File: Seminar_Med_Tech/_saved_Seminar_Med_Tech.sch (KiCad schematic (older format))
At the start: 86 parts, among them U1 JP26, U10 JP27, U11 JP28, U12 JP29, U13 JP30, U14 ADS1298, U15 JP31, U16 JP32, U17 JP33, U18 ADS1298, U19 OPA2340, U2 JP27, U20 J5, U3 JP28, U4 JP29, U5 JP30, U6 JP31, U7 JP32, U8 JP33, U9 JP26

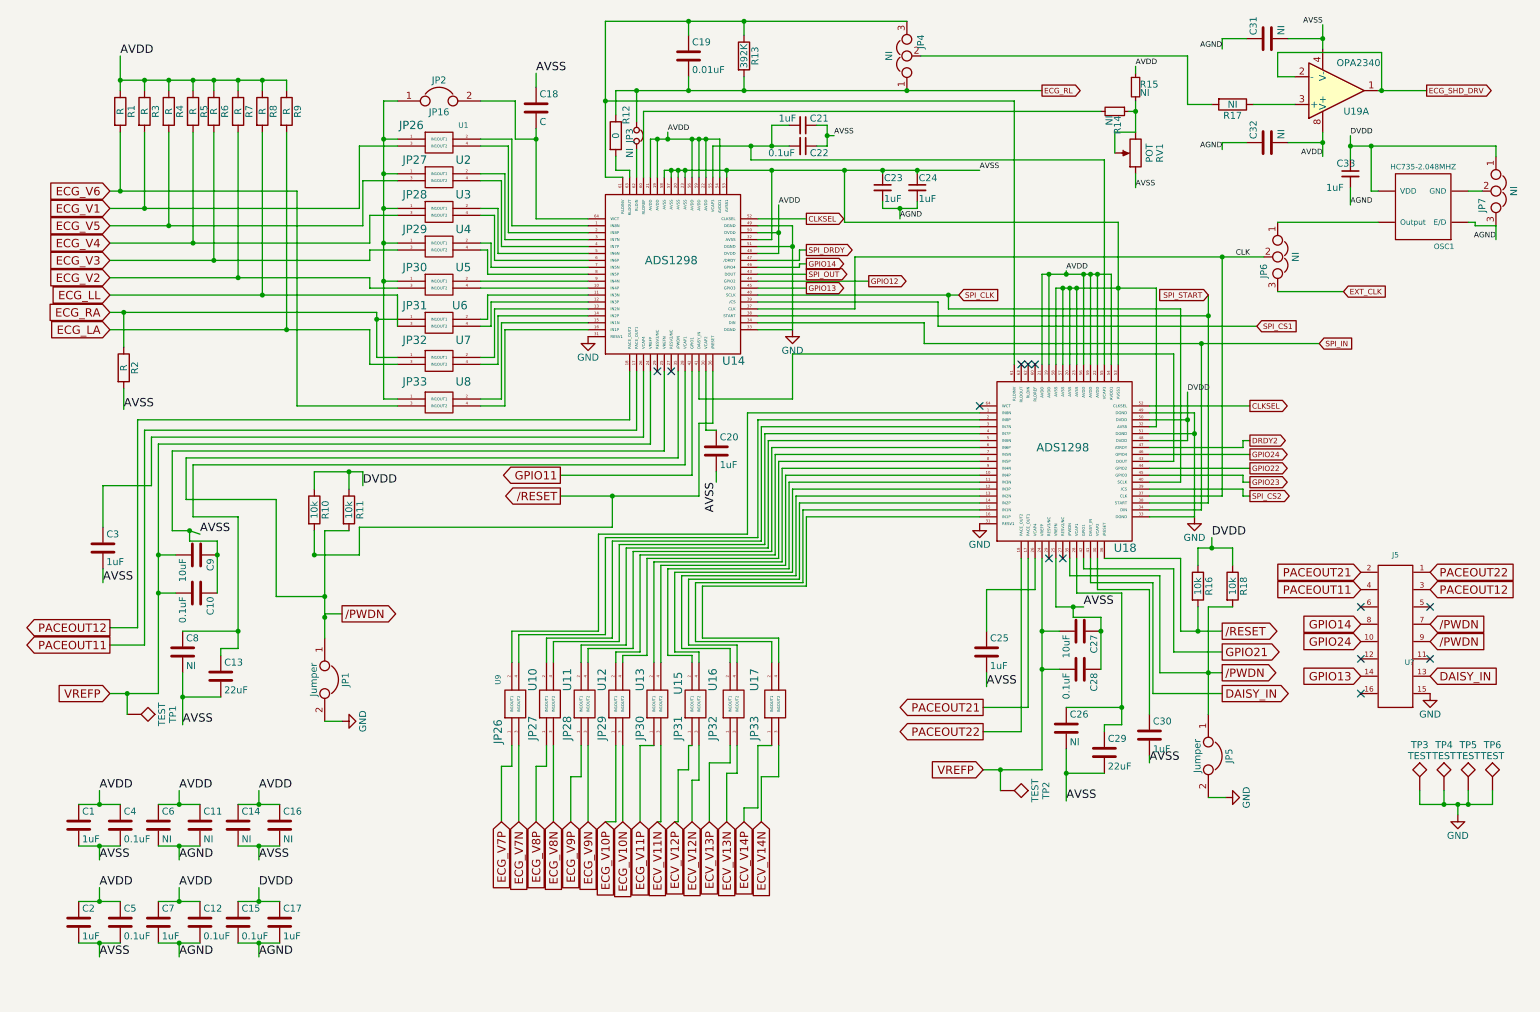
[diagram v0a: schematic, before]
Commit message: Updated Dokumentation and Schaltbild
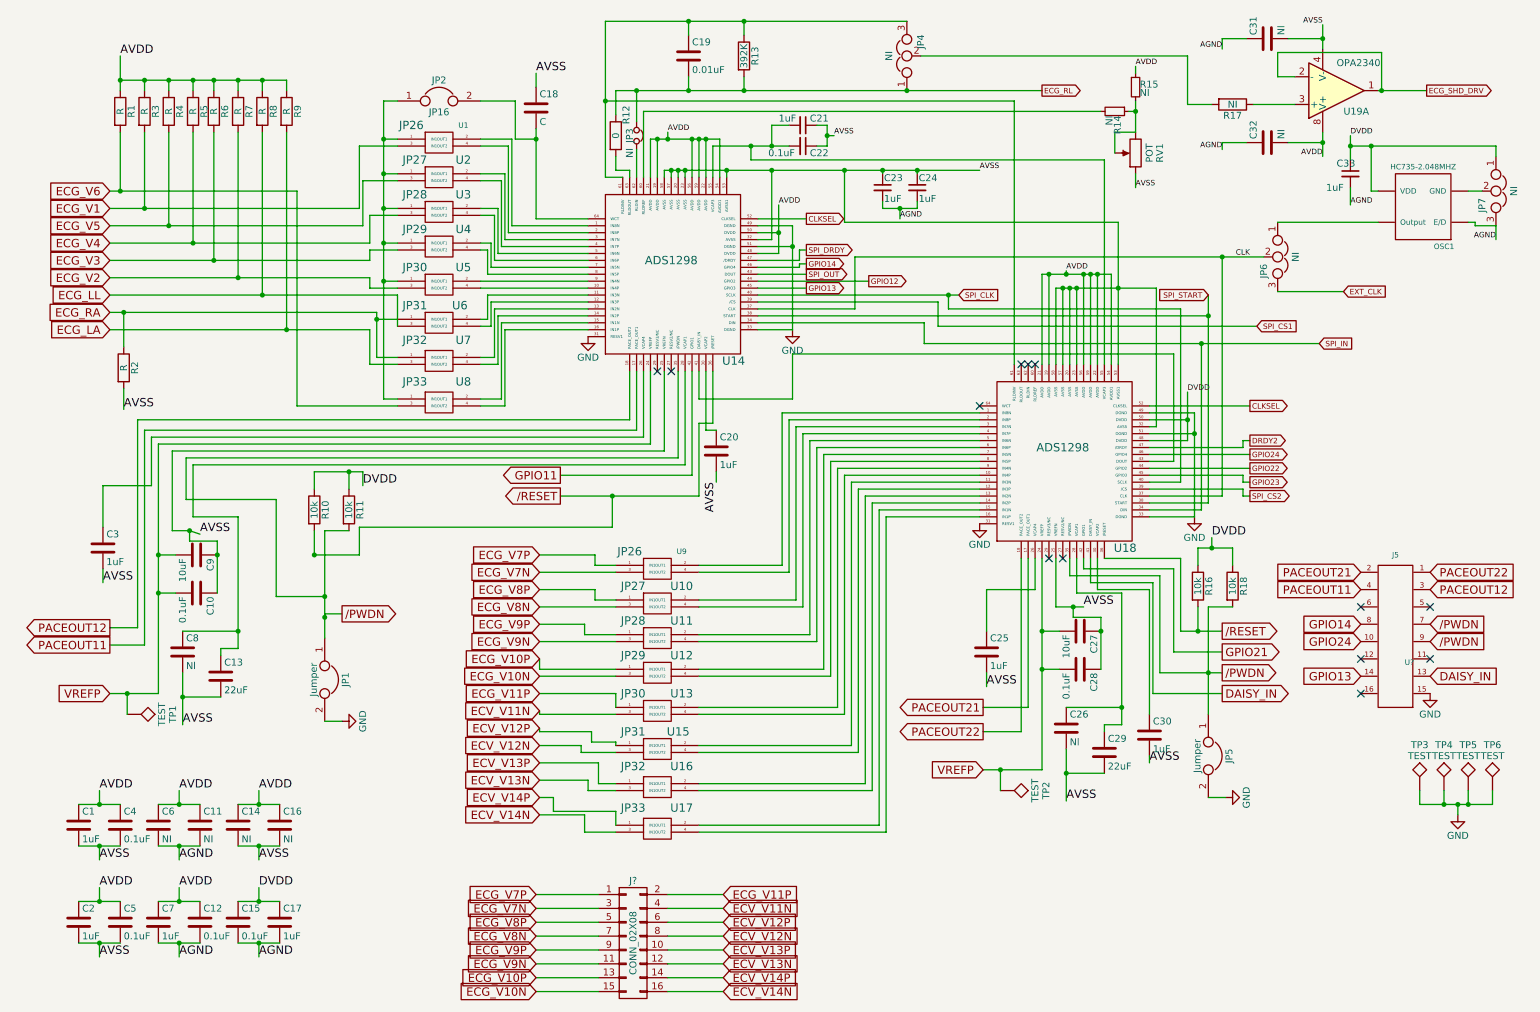
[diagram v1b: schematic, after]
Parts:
- added J?: CONN_02X08, symbol CONN_02X08
- renumbered U20 to U?
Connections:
- net ECG_V10N: now also J?.15 (P15)
- net ECG_V10P: now also J?.13 (P13)
- net ECG_V11P: now also J?.2 (P2)
- net ECG_V7N: now also J?.3 (P3)
- net ECG_V7P: now also J?.1 (P1)
- net ECG_V8N: now also J?.7 (P7)
- net ECG_V8P: now also J?.5 (P5)
- net ECG_V9N: now also J?.11 (P11)
- net ECG_V9P: now also J?.9 (P9)
- net ECV_V11N: now also J?.4 (P4)
- net ECV_V12N: now also J?.8 (P8)
- net ECV_V12P: now also J?.6 (P6)
- net ECV_V13N: now also J?.12 (P12)
- net ECV_V13P: now also J?.10 (P10)
- net ECV_V14N: now also J?.16 (P16)
- net ECV_V14P: now also J?.14 (P14)
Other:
- moved on the sheet: U10, U11, U12, U13, U15, U16, U17, U9

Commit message: Updated
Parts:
- JP1: renamed from JP3; value NI -> Jumper
- JP16: renamed from JP2; value JP16 -> Jumper
- U1: value JP26 -> JP22
- U10: value JP27 -> JP31
- U11: value JP28 -> JP32
- U12: value JP29 -> JP33
- U13: value JP30 -> JP34
- U15: value JP31 -> JP35
- U16: value JP32 -> JP36
- U17: value JP33 -> JP37
- U2: value JP27 -> JP23
- U3: value JP28 -> JP24
- U4: value JP29 -> JP25
- U5: value JP30 -> JP26
- U6: value JP31 -> JP27
- U7: value JP32 -> JP28
- U8: value JP33 -> JP29
- U9: value JP26 -> JP30
- renumbered JP4 to JP17, JP6 to JP18, JP7 to JP19, JP1 to JP4, U14 to U1
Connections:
- net /PWDN: no longer U?.9
- net AGND: now also JP5.2
- net GND: no longer JP5.2
- net SPI_IN: no longer U1.34 (DIN), U18.34 (DIN)
- net WCT: now reaches JP16.1, U1.1 (IN1), U2.1 (IN1), U3.1 (IN1), U4.1 (IN1), U5.1 (IN1), U8.1 (IN1)
- new net: U1.34 (DIN), U18.34 (DIN)
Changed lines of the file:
@@
 $EndDescr
 $Comp
-L Jumper JP2
+L Jumper JP16
 U 1 1 5921B571
 P 3450 1175
-F 0 "JP2" H 3450 1325 50  0000 C CNN
-F 1 "JP16" H 3450 1095 50  0000 C CNN
+F 0 "JP16" H 3450 1325 50  0000 C CNN
+F 1 "Jumper" H 3450 1095 50  0000 C CNN
 F 2 "" H 3450 1175 50  0001 C CNN
 F 3 "" H 3450 1175 50  0001 C CNN
@@
 P 3450 1475
 F 0 "U1" H 3625 1600 39  0000 C CNN
-F 1 "JP26" H 3250 1600 60  0000 C CNN
+F 1 "JP22" H 3250 1600 60  0000 C CNN
 F 2 "" H 3450 1475 60  0001 C CNN
 F 3 "" H 3450 1475 60  0001 C CNN
@@
 P 3450 1725
 F 0 "U2" H 3625 1850 60  0000 C CNN
-F 1 "JP27" H 3275 1850 60  0000 C CNN
+F 1 "JP23" H 3275 1850 60  0000 C CNN
 F 2 "" H 3450 1725 60  0001 C CNN
 F 3 "" H 3450 1725 60  0001 C CNN
@@
 P 3450 1975
 F 0 "U3" H 3625 2100 60  0000 C CNN
-F 1 "JP28" H 3275 2100 60  0000 C CNN
+F 1 "JP24" H 3275 2100 60  0000 C CNN
 F 2 "" H 3450 1975 60  0001 C CNN
 F 3 "" H 3450 1975 60  0001 C CNN
@@
 P 3450 2225
 F 0 "U4" H 3625 2350 60  0000 C CNN
-F 1 "JP29" H 3275 2350 60  0000 C CNN
+F 1 "JP25" H 3275 2350 60  0000 C CNN
 F 2 "" H 3450 2225 60  0001 C CNN
 F 3 "" H 3450 2225 60  0001 C CNN
@@
 P 3450 2500
 F 0 "U5" H 3625 2625 60  0000 C CNN
-F 1 "JP30" H 3275 2625 60  0000 C CNN
+F 1 "JP26" H 3275 2625 60  0000 C CNN
 F 2 "" H 3450 2500 60  0001 C CNN
 F 3 "" H 3450 2500 60  0001 C CNN
@@
 P 3450 2775
 F 0 "U6" H 3600 2900 60  0000 C CNN
-F 1 "JP31" H 3275 2900 60  0000 C CNN
+F 1 "JP27" H 3275 2900 60  0000 C CNN
 F 2 "" H 3450 2775 60  0001 C CNN
 F 3 "" H 3450 2775 60  0001 C CNN
@@
 P 3450 3050
 F 0 "U7" H 3625 3200 60  0000 C CNN
-F 1 "JP32" H 3275 3200 60  0000 C CNN
+F 1 "JP28" H 3275 3200 60  0000 C CNN
 F 2 "" H 3450 3050 60  0001 C CNN
 F 3 "" H 3450 3050 60  0001 C CNN
@@
 P 3450 3350
 F 0 "U8" H 3625 3500 60  0000 C CNN
-F 1 "JP33" H 3275 3500 60  0000 C CNN
+F 1 "JP29" H 3275 3500 60  0000 C CNN
 F 2 "" H 3450 3350 60  0001 C CNN
 F 3 "" H 3450 3350 60  0001 C CNN
@@
 AVSS
 $Comp
-L ADS1298 U14
+L ADS1298 U1
 U 1 1 5921E8FA
 P 5125 2425
-F 0 "U14" H 5575 1800 60  0000 C CNN
+F 0 "U1" H 5575 1800 60  0000 C CNN
 F 1 "ADS1298" H 5125 2525 60  0000 C CNN
 F 2 "" H 5075 2275 60  0001 C CNN
@@
 Text GLabel 9350 2800 2    39   Input ~ 0
 SPI_CS1
-Text GLabel 9800 2925 2    39   Input ~ 0
+Text GLabel 9825 2975 2    39   Input ~ 0
 SPI_IN
 Text GLabel 7200 2575 2    39   Input ~ 0
@@
 	0    1    1    0
 $EndComp
-$Comp
-L GND #PWR6
-U 1 1 592B55D3
-P 9125 6200
-F 0 "#PWR6" H 9125 5950 50  0001 C CNN
-F 1 "GND" H 9125 6050 50  0000 C CNN
-F 2 "" H 9125 6200 50  0001 C CNN
-F 3 "" H 9125 6200 50  0001 C CNN
-	1    9125 6200
-	0    -1   -1   0
-$EndComp
 Text Label 9025 4325 0    60   ~ 0
 DVDD
@@
 $EndComp
 $Comp
-L Jumper JP1
+L Jumper JP4
 U 1 1 592BD318
 P 2625 5350
-F 0 "JP1" H 2625 5500 50  0000 C CNN
+F 0 "JP4" H 2625 5500 50  0000 C CNN
 F 1 "Jumper" H 2625 5270 50  0000 C CNN
 F 2 "" H 2625 5350 50  0001 C CNN
@@
 PACEOUT12
 Text GLabel 10600 4950 2    60   Input ~ 0
-/PWDN
-Text GLabel 10600 5075 2    60   Input ~ 0
 /PWDN
 Text GLabel 10100 4575 0    60   Input ~ 0
@@
 $EndComp
 $Comp
-L Jumper_NC_Dual JP4
+L Jumper_NC_Dual JP17
 U 1 1 59389AEC
 P 6825 850
-F 0 "JP4" H 6875 750 50  0000 L CNN
+F 0 "JP17" H 6875 750 50  0000 L CNN
 F 1 "NI" H 6825 950 50  0000 C BNN
 F 2 "" H 6825 850 50  0001 C CNN
@@
 U 1 1 5938E491
 P 4725 1425
-F 0 "R12" V 4800 1575 50  0000 C CNN
+F 0 "R12" V 4600 1425 50  0000 C CNN
 F 1 "0" V 4725 1425 50  0000 C CNN
 F 2 "" V 4655 1425 50  0001 C CNN
@@
 $EndComp
 $Comp
-L Jumper_NC_Small JP3
+L Jumper_NC_Small JP1
 U 1 1 59391637
 P 4875 1425
-F 0 "JP3" H 4875 1375 50  0000 C CNN
-F 1 "NI" H 5000 1375 50  0000 C CNN
+F 0 "JP1" H 4750 1375 50  0000 C CNN
+F 1 "Jumper" H 5000 1375 50  0000 C CNN
 F 2 "" H 4875 1425 50  0001 C CNN
 F 3 "" H 4875 1425 50  0001 C CNN
@@
 AVSS
 $Comp
-L Jumper_NC_Dual JP6
+L Jumper_NC_Dual JP18
 U 1 1 593C6B14
 P 9500 2300
-F 0 "JP6" H 9550 2200 50  0000 L CNN
+F 0 "JP18" H 9550 2200 50  0000 L CNN
 F 1 "NI" H 9500 2400 50  0000 C BNN
 F 2 "" H 9500 2300 50  0001 C CNN
@@
 $EndComp
 $Comp
-L Jumper_NC_Dual JP7
+L Jumper_NC_Dual JP19
 U 1 1 593CE6F6
 P 11075 1825
-F 0 "JP7" H 11125 1725 50  0000 L CNN
+F 0 "JP19" H 11125 1725 50  0000 L CNN
 F 1 "NI" H 11075 1925 50  0000 C BNN
 F 2 "" H 11075 1825 50  0001 C CNN
@@
 P 5025 4550
 F 0 "U9" H 5200 4675 39  0000 C CNN
-F 1 "JP26" H 4825 4675 60  0000 C CNN
+F 1 "JP30" H 4825 4675 60  0000 C CNN
 F 2 "" H 5025 4550 60  0001 C CNN
 F 3 "" H 5025 4550 60  0001 C CNN
@@
 P 5025 4800
 F 0 "U10" H 5200 4925 60  0000 C CNN
-F 1 "JP27" H 4850 4925 60  0000 C CNN
+F 1 "JP31" H 4850 4925 60  0000 C CNN
 F 2 "" H 5025 4800 60  0001 C CNN
 F 3 "" H 5025 4800 60  0001 C CNN
@@
 P 5025 5050
 F 0 "U11" H 5200 5175 60  0000 C CNN
-F 1 "JP28" H 4850 5175 60  0000 C CNN
+F 1 "JP32" H 4850 5175 60  0000 C CNN
 F 2 "" H 5025 5050 60  0001 C CNN
 F 3 "" H 5025 5050 60  0001 C CNN
@@
 P 5025 5300
 F 0 "U12" H 5200 5425 60  0000 C CNN
-F 1 "JP29" H 4850 5425 60  0000 C CNN
+F 1 "JP33" H 4850 5425 60  0000 C CNN
 F 2 "" H 5025 5300 60  0001 C CNN
 F 3 "" H 5025 5300 60  0001 C CNN
@@
 P 5025 5575
 F 0 "U13" H 5200 5700 60  0000 C CNN
-F 1 "JP30" H 4850 5700 60  0000 C CNN
+F 1 "JP34" H 4850 5700 60  0000 C CNN
 F 2 "" H 5025 5575 60  0001 C CNN
 F 3 "" H 5025 5575 60  0001 C CNN
@@
 P 5025 5850
 F 0 "U15" H 5175 5975 60  0000 C CNN
-F 1 "JP31" H 4850 5975 60  0000 C CNN
+F 1 "JP35" H 4850 5975 60  0000 C CNN
 F 2 "" H 5025 5850 60  0001 C CNN
 F 3 "" H 5025 5850 60  0001 C CNN
@@
 P 5025 6125
 F 0 "U16" H 5200 6275 60  0000 C CNN
-F 1 "JP32" H 4850 6275 60  0000 C CNN
+F 1 "JP36" H 4850 6275 60  0000 C CNN
 F 2 "" H 5025 6125 60  0001 C CNN
 F 3 "" H 5025 6125 60  0001 C CNN
@@
 P 5025 6425
 F 0 "U17" H 5200 6575 60  0000 C CNN
-F 1 "JP33" H 4850 6575 60  0000 C CNN
+F 1 "JP37" H 4850 6575 60  0000 C CNN
 F 2 "" H 5025 6425 60  0001 C CNN
 F 3 "" H 5025 6425 60  0001 C CNN
@@
 	6950 2925 8950 2925
 Wire Wire Line
-	8950 2925 9800 2925
+	8975 2975 9825 2975
 Connection ~ 8950 2925
 Wire Wire Line
@@
 Wire Wire Line
 	5100 7600 5500 7600
+Text Label 9125 6200 0    60   ~ 0
+AGND
+Text Label 3050 1175 0    60   ~ 0
+WCT
 $EndSCHEMATC
